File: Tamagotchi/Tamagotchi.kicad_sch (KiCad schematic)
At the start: 15 parts, among them SW1 SW_Push, SW2 SW_Push, SW3 SW_Push, U1 XIAO-ESP32-C6-DIP, U2 DM-OLED096-636

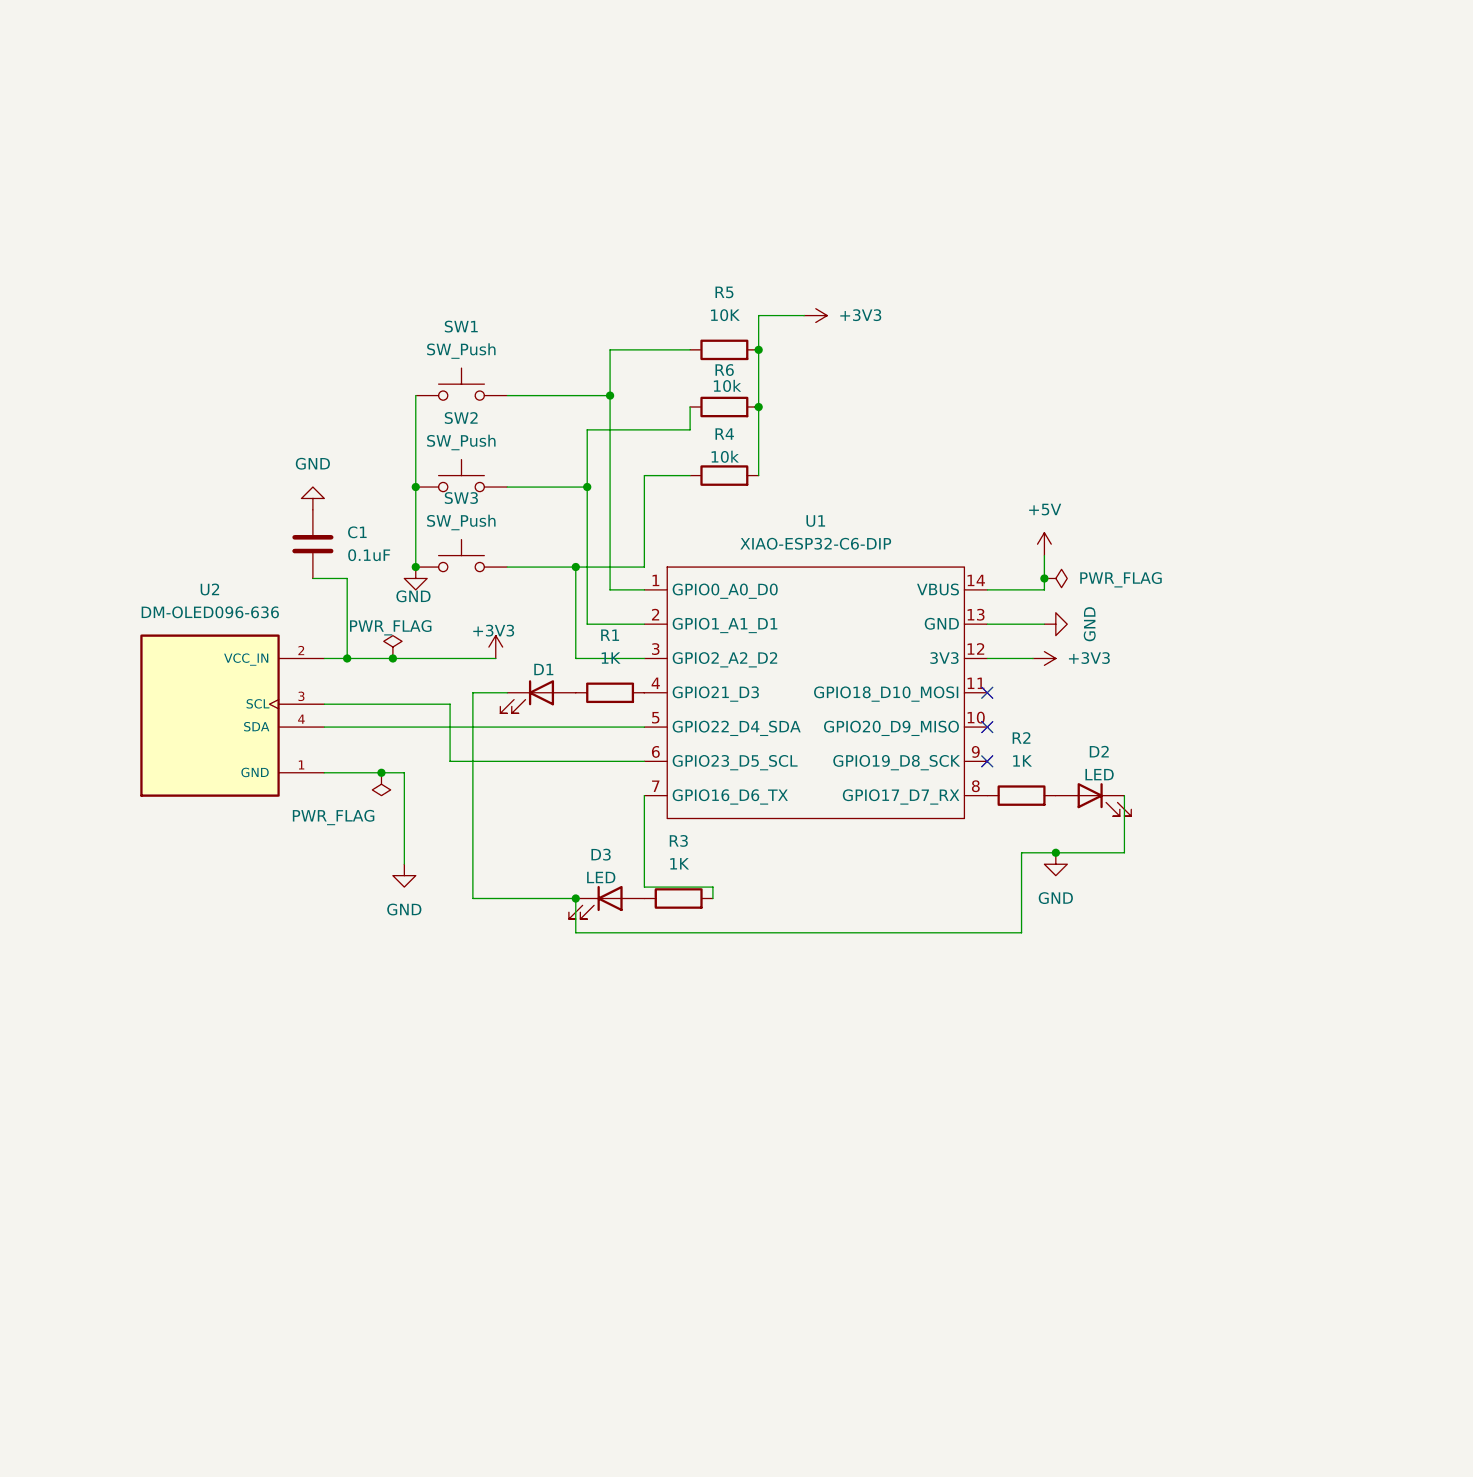
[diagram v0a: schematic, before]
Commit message: had to rewire pcb due to changing the esp32
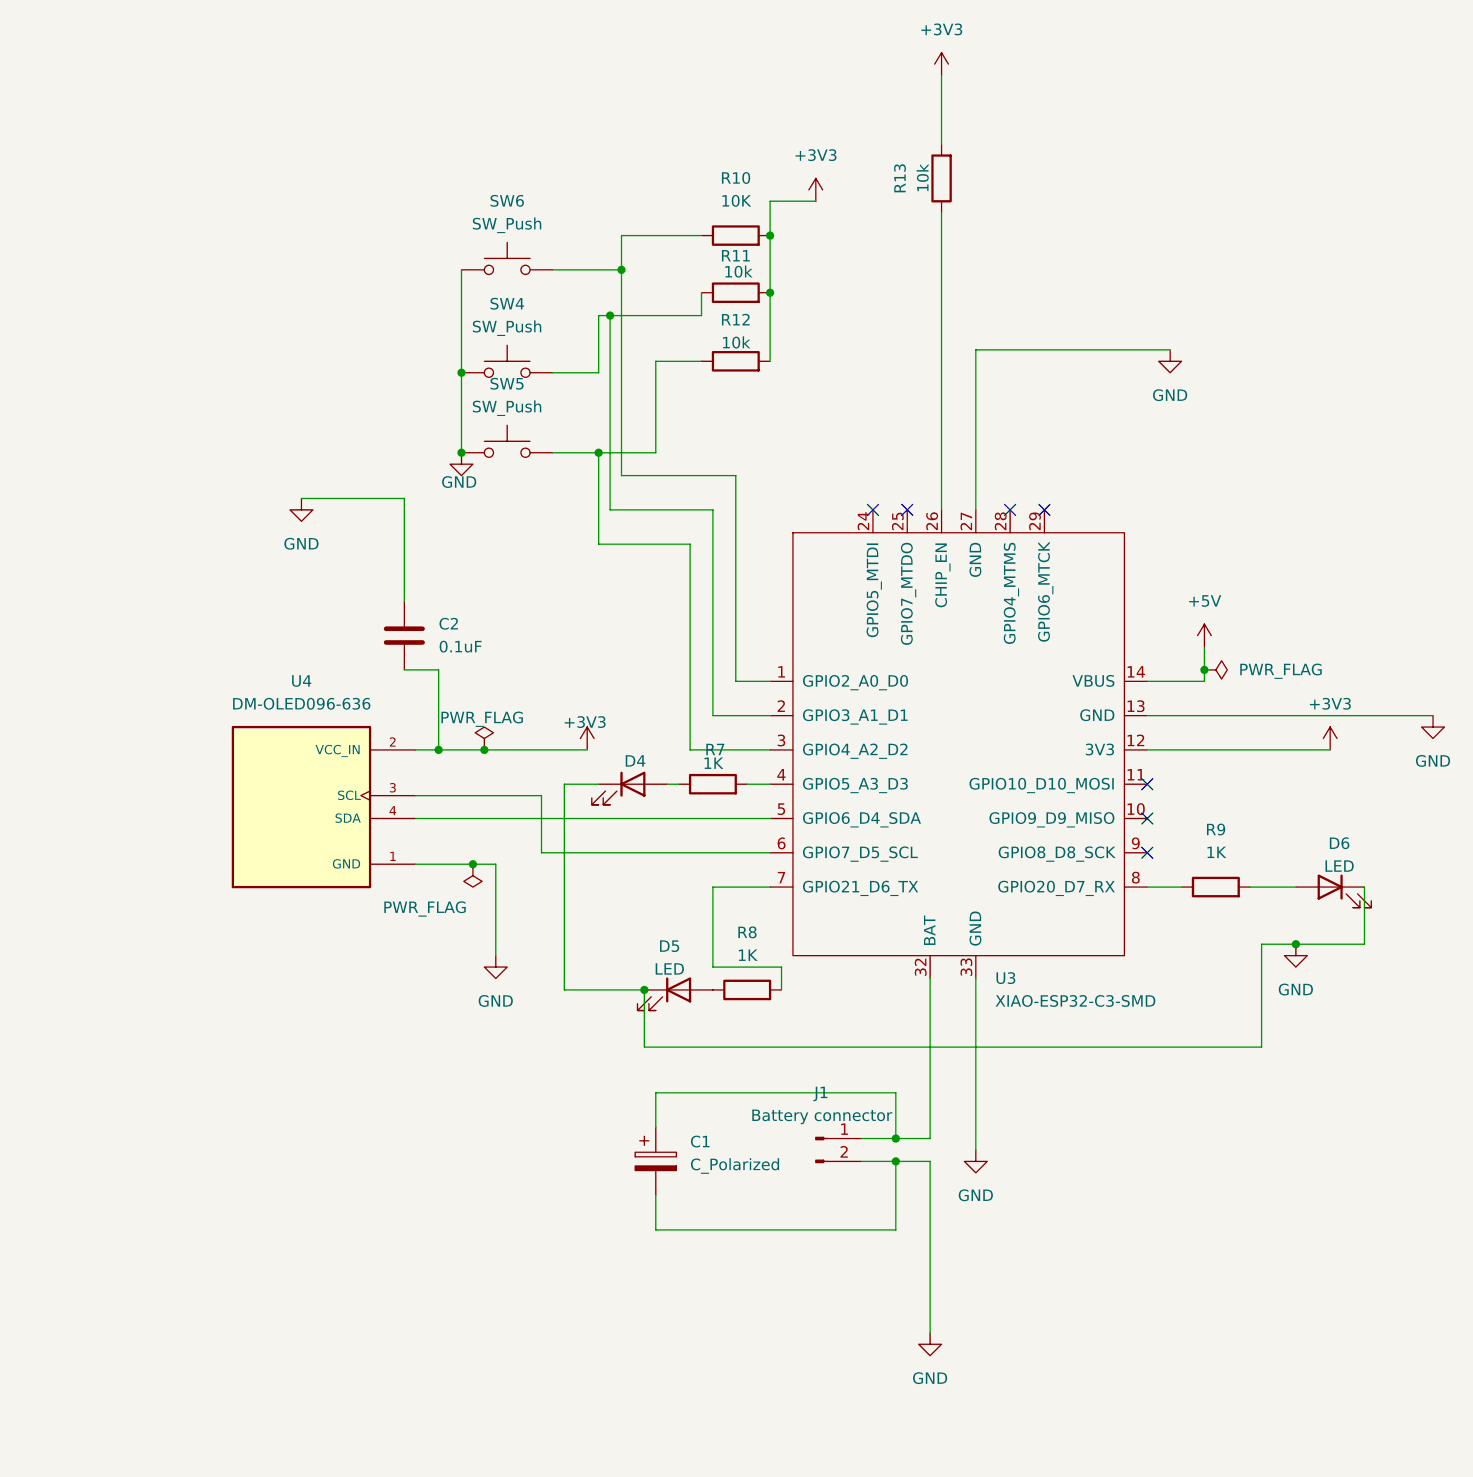
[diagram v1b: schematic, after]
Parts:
- removed C1: 0.1uF, Capacitor_SMD:C_0805_2012Metric, symbol Device:C
- removed D1, D2, D3: LED, LED_THT:LED_D1.8mm_W1.8mm_H2.4mm_Horizontal_O1.27mm_Z1.6mm, symbol Device:LED
- removed R1, R2, R3: 1K, Resistor_SMD:R_0805_2012Metric, symbol Device:R
- removed R4, R6: 10k, Resistor_SMD:R_0805_2012Metric, symbol Device:R
- removed R5: 10K, Resistor_SMD:R_0805_2012Metric, symbol Device:R
- removed SW1, SW2, SW3: SW_Push, Button_Switch_THT:KSA_Tactile_SPST, symbol Switch:SW_Push
- removed U1: XIAO-ESP32-C6-DIP, Seeed Studio XIAO Series Library:XIAO-ESP32-C6-DIP, symbol Seeed_Studio_XIAO_Series:XIAO-ESP32-C6-DIP
- removed U2: DM-OLED096-636, DM-OLED096-636 (1):MODULE_DM-OLED096-636, symbol DM-OLED096-636:DM-OLED096-636
- added C1: C_Polarized, Capacitor_SMD:C_0805_2012Metric, symbol Device:C_Polarized
- added C2: 0.1uF, Capacitor_SMD:C_0805_2012Metric, symbol Device:C
- added D4, D5, D6: LED, LED_THT:LED_D1.8mm_W1.8mm_H2.4mm_Horizontal_O1.27mm_Z1.6mm, symbol Device:LED
- added J1: Battery connector, Connector_JST:JST_GH_BM02B-GHS-TBT_1x02-1MP_P1.25mm_Vertical, symbol Connector:Conn_01x02_Pin
- added R10: 10K, Resistor_SMD:R_0805_2012Metric, symbol Device:R
- added R11, R12, R13: 10k, Resistor_SMD:R_0805_2012Metric, symbol Device:R
- added R7, R8, R9: 1K, Resistor_SMD:R_0805_2012Metric, symbol Device:R
- added SW4, SW5, SW6: SW_Push, Button_Switch_THT:KSA_Tactile_SPST, symbol Switch:SW_Push
- added U3: XIAO-ESP32-C3-SMD, Seeed Studio XIAO Series Library:XIAO-ESP32-C3-SMD, symbol Seeed_Studio_XIAO_Series:XIAO-ESP32-C3-SMD
- added U4: DM-OLED096-636, DM-OLED096-636 (1):MODULE_DM-OLED096-636, symbol DM-OLED096-636:DM-OLED096-636
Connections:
- net +3V3: now also C2.1, R10.2, R11.2, R12.2, R13.2, U3.12 (3V3), U4.2 (VCC_IN)
- net +5V: now also U3.14 (VBUS)
- net GND: now also C1.2, C2.2, D4.1 (K), D5.1 (K), D6.1 (K), J1.2 (Pin_2), SW4.1, SW5.1, SW6.1, U3.13 (GND), U3.27 (GND), U3.33 (GND), U4.1 (GND)
- new net: R11.1, SW4.2, U3.2 (GPIO3_A1_D1)
- new net: D5.2 (A), R8.1
- new net: R8.2, U3.7 (GPIO21_D6_TX)
- new net: R12.1, SW5.2, U3.3 (GPIO4_A2_D2)
- new net: C1.1, J1.1 (Pin_1), U3.32 (BAT)
- new net: R10.1, SW6.2, U3.1 (GPIO2_A0_D0)
- new net: R13.1, U3.26 (CHIP_EN)
- new net: R7.2, U3.4 (GPIO5_A3_D3)
- new net: U3.5 (GPIO6_D4_SDA), U4.4 (SDA)
- new net: U3.6 (GPIO7_D5_SCL), U4.3 (SCL)
- new net: R9.1, U3.8 (GPIO20_D7_RX)
- new net: D4.2 (A), R7.1
- new net: D6.2 (A), R9.2
- no-connect marks 3 -> 7

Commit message: have so much to fixxx
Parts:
- removed J1: Battery connector, Connector_JST:JST_GH_BM02B-GHS-TBT_1x02-1MP_P1.25mm_Vertical, symbol Connector:Conn_01x02_Pin
- added BT1: Battery_Cell, Battery:BatteryHolder_Keystone_3034_1x20mm, symbol Device:Battery_Cell
- C1: value C_Polarized -> 100uF
- SW4, SW5, SW6: footprint Button_Switch_THT:KSA_Tactile_SPST -> Button_Switch_THT:SW_PUSH_6mm_H5mm
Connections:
- net GND: now also BT1.2 (-); no longer C1.2
- net at U3.32 (BAT): now also BT1.1 (+); no longer C1.1
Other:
- moved on the sheet: C1
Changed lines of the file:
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@@
 	)
 	(junction
-		(at 157.48 140.97)
-		(diameter 0)
-		(color 0 0 0 0)
-	)
-	(junction
-		(at 157.48 143.51)
-		(diameter 0)
-		(color 0 0 0 0)
-	)
-	(junction
 		(at 143.51 46.99)
 		(diameter 0)
@@
 	(wire
 		(pts
-			(xy 157.48 143.51) (xy 157.48 151.13)
+			(xy 88.9 138.43) (xy 88.9 146.05)
 		)
 		(stroke
@@
 	(wire
 		(pts
-			(xy 157.48 151.13) (xy 130.81 151.13)
+			(xy 88.9 146.05) (xy 62.23 146.05)
 		)
 		(stroke
@@
 	(wire
 		(pts
+			(xy 139.7 146.05) (xy 157.48 146.05)
+		)
+		(stroke
+			(width 0)
+			(type default)
+		)
+	)
+	(wire
+		(pts
 			(xy 127 67.31) (xy 139.7 67.31)
 		)
@@
 	(wire
 		(pts
-			(xy 130.81 135.89) (xy 157.48 135.89)
+			(xy 62.23 130.81) (xy 88.9 130.81)
 		)
 		(stroke
@@
 	(wire
 		(pts
+			(xy 139.7 138.43) (xy 157.48 138.43)
+		)
+		(stroke
+			(width 0)
+			(type default)
+		)
+	)
+	(wire
+		(pts
 			(xy 166.37 53.34) (xy 166.37 71.12)
 		)
@@
 	(wire
 		(pts
+			(xy 157.48 138.43) (xy 157.48 140.97)
+		)
+		(stroke
+			(width 0)
+			(type default)
+		)
+	)
+	(wire
+		(pts
 			(xy 143.51 46.99) (xy 143.51 40.64)
 		)
@@
 	(wire
 		(pts
-			(xy 130.81 139.7) (xy 130.81 135.89)
+			(xy 62.23 134.62) (xy 62.23 130.81)
 		)
 		(stroke
@@
 	(wire
 		(pts
-			(xy 157.48 135.89) (xy 157.48 140.97)
+			(xy 88.9 130.81) (xy 88.9 135.89)
 		)
 		(stroke
@@
 	(wire
 		(pts
-			(xy 153.67 140.97) (xy 157.48 140.97)
+			(xy 85.09 135.89) (xy 88.9 135.89)
 		)
 		(stroke
@@
 	(wire
 		(pts
-			(xy 130.81 147.32) (xy 130.81 151.13)
+			(xy 62.23 142.24) (xy 62.23 146.05)
 		)
 		(stroke
@@
 	(wire
 		(pts
-			(xy 153.67 143.51) (xy 157.48 143.51)
+			(xy 85.09 138.43) (xy 88.9 138.43)
 		)
 		(stroke
@@
 	(wire
 		(pts
+			(xy 157.48 143.51) (xy 157.48 146.05)
+		)
+		(stroke
+			(width 0)
+			(type default)
+		)
+	)
+	(wire
+		(pts
 			(xy 119.38 64.77) (xy 124.46 64.77)
 		)
@@
 			)
 		)
-		(property "Footprint" "Button_Switch_THT:KSA_Tactile_SPST"
+		(property "Footprint" "Button_Switch_THT:SW_PUSH_6mm_H5mm"
 			(at 114.3 50.8 0)
 			(hide yes)
@@
 			)
 		)
-		(property "Footprint" "Button_Switch_THT:KSA_Tactile_SPST"
+		(property "Footprint" "Button_Switch_THT:SW_PUSH_6mm_H5mm"
 			(at 114.3 59.69 0)
 			(hide yes)
@@
 	)
 	(symbol
-		(lib_id "Connector:Conn_01x02_Pin")
-		(at 148.59 140.97 0)
-		(unit 1)
-		(body_style 1)
-		(exclude_from_sim no)
-		(in_bom yes)
-		(on_board yes)
-		(in_pos_files yes)
-		(dnp no)
-		(fields_autoplaced yes)
-		(property "Reference" "J1"
-			(at 149.225 135.89 0)
-			(show_name no)
-			(do_not_autoplace no)
-			(effects
-				(font
-					(size 1.27 1.27)
-				)
-			)
-		)
-		(property "Value" "Battery connector"
-			(at 149.225 138.43 0)
-			(show_name no)
-			(do_not_autoplace no)
-			(effects
-				(font
-					(size 1.27 1.27)
-				)
-			)
-		)
-		(property "Footprint" "Connector_JST:JST_GH_BM02B-GHS-TBT_1x02-1MP_P1.25mm_Vertical"
-			(at 148.59 140.97 0)
-			(hide yes)
-			(show_name no)
-			(do_not_autoplace no)
-			(effects
-				(font
-					(size 1.27 1.27)
-				)
-			)
-		)
-		(property "Datasheet" ""
-			(at 148.59 140.97 0)
-			(hide yes)
-			(show_name no)
-			(do_not_autoplace no)
-			(effects
-				(font
-					(size 1.27 1.27)
-				)
-			)
-		)
-		(property "Description" "Generic connector, single row, 01x02, script generated"
-			(at 148.59 140.97 0)
-			(hide yes)
-			(show_name no)
-			(do_not_autoplace no)
-			(effects
-				(font
-					(size 1.27 1.27)
-				)
-			)
-		)
-		(pin "2"
-		)
-		(pin "1"
-		)
-		(instances
-			(project "Tamagotchi"
-				(path "/dd5d29a8-0ca1-4c75-a105-470d6b907a46"
-					(reference "J1")
-					(unit 1)
-				)
-			)
-		)
-	)
-	(symbol
 		(lib_id "Seeed_Studio_XIAO_Series:XIAO-ESP32-C3-SMD")
 		(at 165.1 93.98 0)
@@
 			)
 		)
-		(property "Footprint" "Button_Switch_THT:KSA_Tactile_SPST"
+		(property "Footprint" "Button_Switch_THT:SW_PUSH_6mm_H5mm"
 			(at 114.3 39.37 0)
 			(hide yes)
@@
 	(symbol
 		(lib_id "Device:C_Polarized")
-		(at 130.81 143.51 0)
+		(at 62.23 138.43 0)
 		(unit 1)
 		(body_style 1)
@@
 		(fields_autoplaced yes)
 		(property "Reference" "C1"
-			(at 134.62 141.3509 0)
+			(at 66.04 136.2709 0)
 			(show_name no)
 			(do_not_autoplace no)
@@
 			)
 		)
-		(property "Value" "C_Polarized"
-			(at 134.62 143.8909 0)
+		(property "Value" "100uF"
+			(at 66.04 138.8109 0)
 			(show_name no)
 			(do_not_autoplace no)
@@
 		)
 		(property "Footprint" "Capacitor_SMD:C_0805_2012Metric"
-			(at 131.7752 147.32 0)
+			(at 63.1952 142.24 0)
 			(hide yes)
 			(show_name no)
@@
 		)
 		(property "Datasheet" ""
-			(at 130.81 143.51 0)
+			(at 62.23 138.43 0)
 			(hide yes)
 			(show_name no)
@@
 		)
 		(property "Description" "Polarized capacitor"
-			(at 130.81 143.51 0)
+			(at 62.23 138.43 0)
 			(hide yes)
 			(show_name no)
@@
 					(unit 1)
 				)
+			)
+		)
+	)
+	(symbol
+		(lib_id "Device:Battery_Cell")
+		(at 139.7 143.51 0)
+		(mirror y)
+		(unit 1)
+		(body_style 1)
+		(exclude_from_sim no)
+		(in_bom yes)
+		(on_board yes)
+		(in_pos_files yes)
+		(dnp no)
+		(property "Reference" "BT1"
+			(at 135.89 140.3984 0)
+			(show_name no)
+			(do_not_autoplace no)
+			(effects
+				(font
+					(size 1.27 1.27)
+				)
+				(justify left)
+			)
+		)
+		(property "Value" "Battery_Cell"
+			(at 135.89 142.9384 0)
+			(show_name no)
+			(do_not_autoplace no)
+			(effects
+				(font
+					(size 1.27 1.27)
+				)
+				(justify left)
+			)
+		)
+		(property "Footprint" "Battery:BatteryHolder_Keystone_3034_1x20mm"
+			(at 139.7 141.986 90)
+			(hide yes)
+			(show_name no)
+			(do_not_autoplace no)
+			(effects
+				(font
+					(size 1.27 1.27)
+				)
+			)
+		)
+		(property "Datasheet" ""
+			(at 139.7 141.986 90)
+			(hide yes)
+			(show_name no)
+			(do_not_autoplace no)
+			(effects
+				(font
+					(size 1.27 1.27)
+				)
+			)
+		)
+		(property "Description" "Single-cell battery"
+			(at 139.7 143.51 0)
+			(hide yes)
+			(show_name no)
+			(do_not_autoplace no)
+			(effects
+				(font
+					(size 1.27 1.27)
+				)
+			)
+		)
+		(property "Sim.Device" "V"
+			(at 139.7 143.51 0)
+			(hide yes)
+			(show_name no)
+			(do_not_autoplace no)
+			(effects
+				(font
+					(size 1.27 1.27)
+				)
+			)
+		)
+		(property "Sim.Type" "DC"
+			(at 139.7 143.51 0)
+			(hide yes)
+			(show_name no)
+			(do_not_autoplace no)
+			(effects
+				(font
+					(size 1.27 1.27)
+				)
+			)
+		)
+		(property "Sim.Pins" "1=+ 2=-"
+			(at 139.7 143.51 0)
+			(hide yes)
+			(show_name no)
+			(do_not_autoplace no)
+			(effects
+				(font
+					(size 1.27 1.27)
+				)
+			)
+		)
+		(pin "1"
+		)
+		(pin "2"
+		)
+		(instances
+			(project "Tamagotchi"
+				(path "/dd5d29a8-0ca1-4c75-a105-470d6b907a46"
+					(reference "BT1")
+					(unit 1)
+				)

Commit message: just saving some things last min
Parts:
- removed C1: 100uF, Capacitor_SMD:C_0805_2012Metric, symbol Device:C_Polarized
- BT1: footprint Battery:BatteryHolder_Keystone_3034_1x20mm -> Battery:Battery_Panasonic_CR2032-VS1N_Vertical_CircularHoles
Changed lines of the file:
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@@
 	(wire
 		(pts
-			(xy 88.9 138.43) (xy 88.9 146.05)
-		)
-		(stroke
-			(width 0)
-			(type default)
-		)
-	)
-	(wire
-		(pts
 			(xy 91.44 69.85) (xy 102.87 69.85)
 		)
@@
 	(wire
 		(pts
-			(xy 88.9 146.05) (xy 62.23 146.05)
-		)
-		(stroke
-			(width 0)
-			(type default)
-		)
-	)
-	(wire
-		(pts
 			(xy 139.7 67.31) (xy 139.7 90.17)
 		)
@@
 	(wire
 		(pts
-			(xy 62.23 130.81) (xy 88.9 130.81)
-		)
-		(stroke
-			(width 0)
-			(type default)
-		)
-	)
-	(wire
-		(pts
 			(xy 110.49 110.49) (xy 113.03 110.49)
 		)
@@
 	(wire
 		(pts
-			(xy 62.23 134.62) (xy 62.23 130.81)
-		)
-		(stroke
-			(width 0)
-			(type default)
-		)
-	)
-	(wire
-		(pts
 			(xy 137.16 71.12) (xy 137.16 93.98)
 		)
@@
 	(wire
 		(pts
-			(xy 88.9 130.81) (xy 88.9 135.89)
-		)
-		(stroke
-			(width 0)
-			(type default)
-		)
-	)
-	(wire
-		(pts
 			(xy 124.46 64.77) (xy 124.46 74.93)
 		)
@@
 	(wire
 		(pts
-			(xy 85.09 135.89) (xy 88.9 135.89)
-		)
-		(stroke
-			(width 0)
-			(type default)
-		)
-	)
-	(wire
-		(pts
-			(xy 62.23 142.24) (xy 62.23 146.05)
-		)
-		(stroke
-			(width 0)
-			(type default)
-		)
-	)
-	(wire
-		(pts
-			(xy 85.09 138.43) (xy 88.9 138.43)
-		)
-		(stroke
-			(width 0)
-			(type default)
-		)
-	)
-	(wire
-		(pts
 			(xy 127 44.45) (xy 127 67.31)
 		)
@@
 	)
 	(symbol
-		(lib_id "Device:C_Polarized")
-		(at 62.23 138.43 0)
-		(unit 1)
-		(body_style 1)
-		(exclude_from_sim no)
-		(in_bom yes)
-		(on_board yes)
-		(in_pos_files yes)
-		(dnp no)
-		(fields_autoplaced yes)
-		(property "Reference" "C1"
-			(at 66.04 136.2709 0)
-			(show_name no)
-			(do_not_autoplace no)
-			(effects
-				(font
-					(size 1.27 1.27)
-				)
-				(justify left)
-			)
-		)
-		(property "Value" "100uF"
-			(at 66.04 138.8109 0)
-			(show_name no)
-			(do_not_autoplace no)
-			(effects
-				(font
-					(size 1.27 1.27)
-				)
-				(justify left)
-			)
-		)
-		(property "Footprint" "Capacitor_SMD:C_0805_2012Metric"
-			(at 63.1952 142.24 0)
-			(hide yes)
-			(show_name no)
-			(do_not_autoplace no)
-			(effects
-				(font
-					(size 1.27 1.27)
-				)
-			)
-		)
-		(property "Datasheet" ""
-			(at 62.23 138.43 0)
-			(hide yes)
-			(show_name no)
-			(do_not_autoplace no)
-			(effects
-				(font
-					(size 1.27 1.27)
-				)
-			)
-		)
-		(property "Description" "Polarized capacitor"
-			(at 62.23 138.43 0)
-			(hide yes)
-			(show_name no)
-			(do_not_autoplace no)
-			(effects
-				(font
-					(size 1.27 1.27)
-				)
-			)
-		)
-		(pin "2"
-		)
-		(pin "1"
-		)
-		(instances
-			(project "Tamagotchi"
-				(path "/dd5d29a8-0ca1-4c75-a105-470d6b907a46"
-					(reference "C1")
-					(unit 1)
-				)
-			)
-		)
-	)
-	(symbol
 		(lib_id "Device:C")
 		(at 102.87 85.09 180)
@@
 			)
 		)
-		(property "Footprint" "Battery:BatteryHolder_Keystone_3034_1x20mm"
+		(property "Footprint" "Battery:Battery_Panasonic_CR2032-VS1N_Vertical_CircularHoles"
 			(at 139.7 141.986 90)
 			(hide yes)

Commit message: finally figured out battery
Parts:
- removed BT1: Battery_Cell, Battery:Battery_Panasonic_CR2032-VS1N_Vertical_CircularHoles, symbol Device:Battery_Cell
- added J1: Battery connector, Connector_PinHeader_2.54mm:PinHeader_1x02_P2.54mm_Vertical, symbol Connector:Conn_01x02_Pin
- added J2: Programing, Connector_PinHeader_2.54mm:PinHeader_1x04_P2.54mm_Vertical, symbol Connector:Conn_01x04_Pin
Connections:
- net GND: now also J1.2 (Pin_2)
- net at U3.24 (GPIO5_MTDI): now also J2.4 (Pin_4)
- net at U3.25 (GPIO7_MTDO): now also J2.3 (Pin_3)
- net at U3.28 (GPIO4_MTMS): now also J2.2 (Pin_2)
- net at U3.29 (GPIO6_MTCK): now also J2.1 (Pin_1)
- net at U3.32 (BAT): now also J1.1 (Pin_1)
- no-connect marks 7 -> 3
